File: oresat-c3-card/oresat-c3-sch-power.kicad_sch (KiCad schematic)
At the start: 68 parts, among them U31 LP2985AIM5-3.3, U34 TPS259621DDA, U35 TPS259620DDA, U36 LTC3624-5, U38 LP2985AIM5-3.3, U6 LTC3624-5

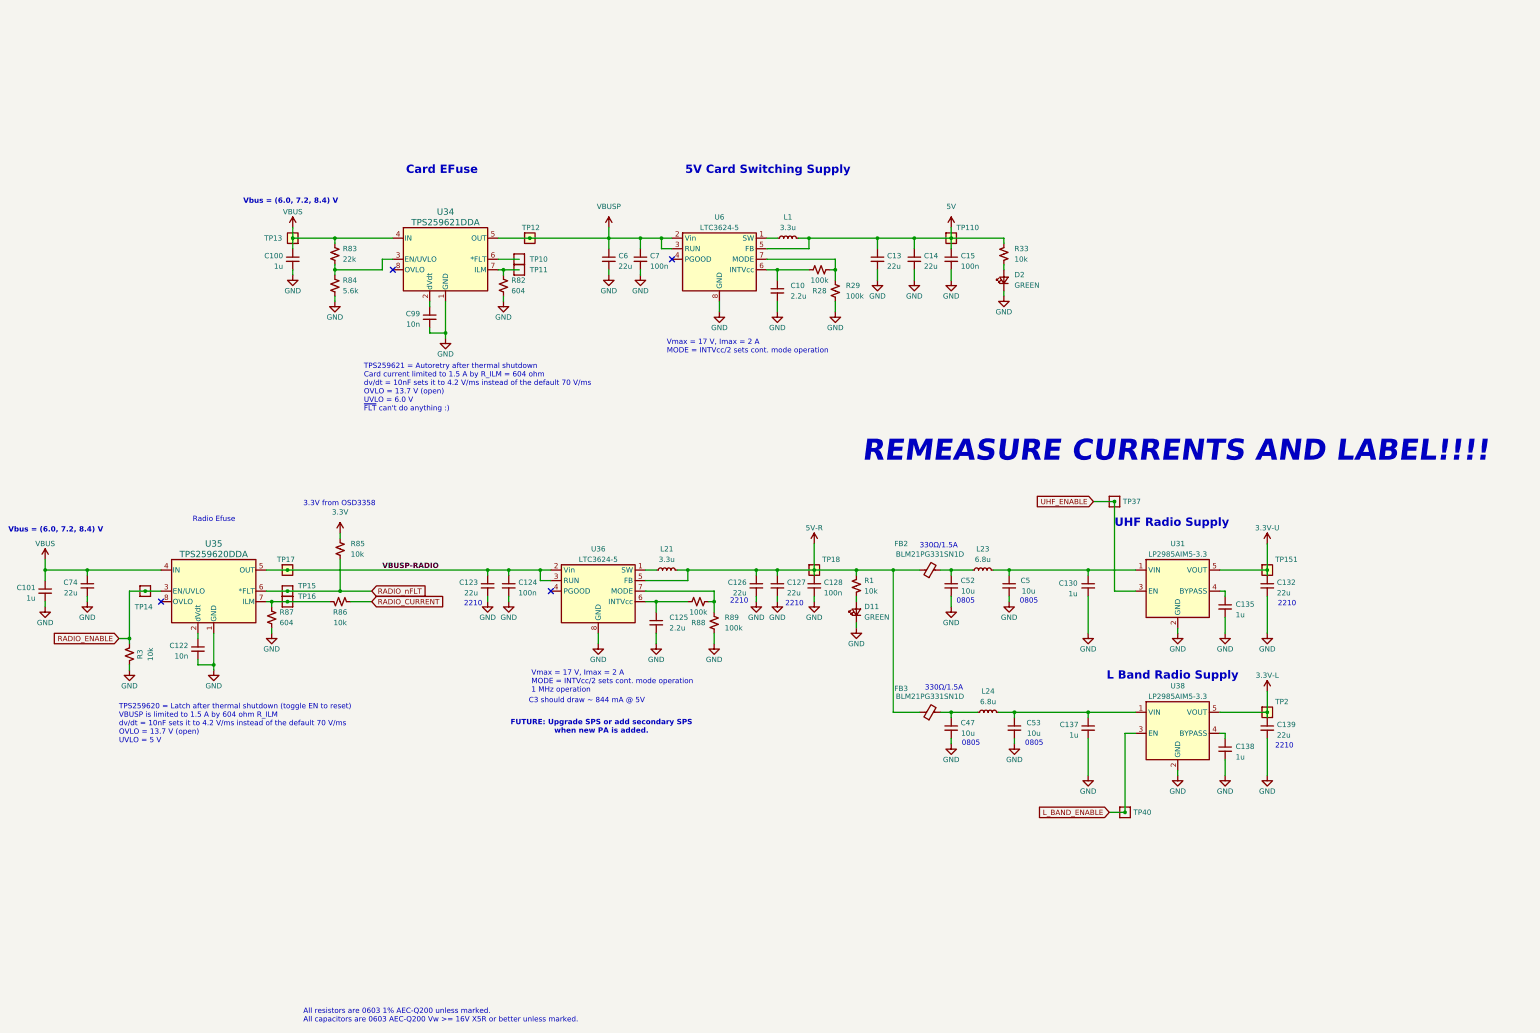
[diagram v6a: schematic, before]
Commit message: Updating BOM and switching to oresat-passive footprints. Fixed some power cutoff limits, and fixed another DC voltage leverl on an LNA!
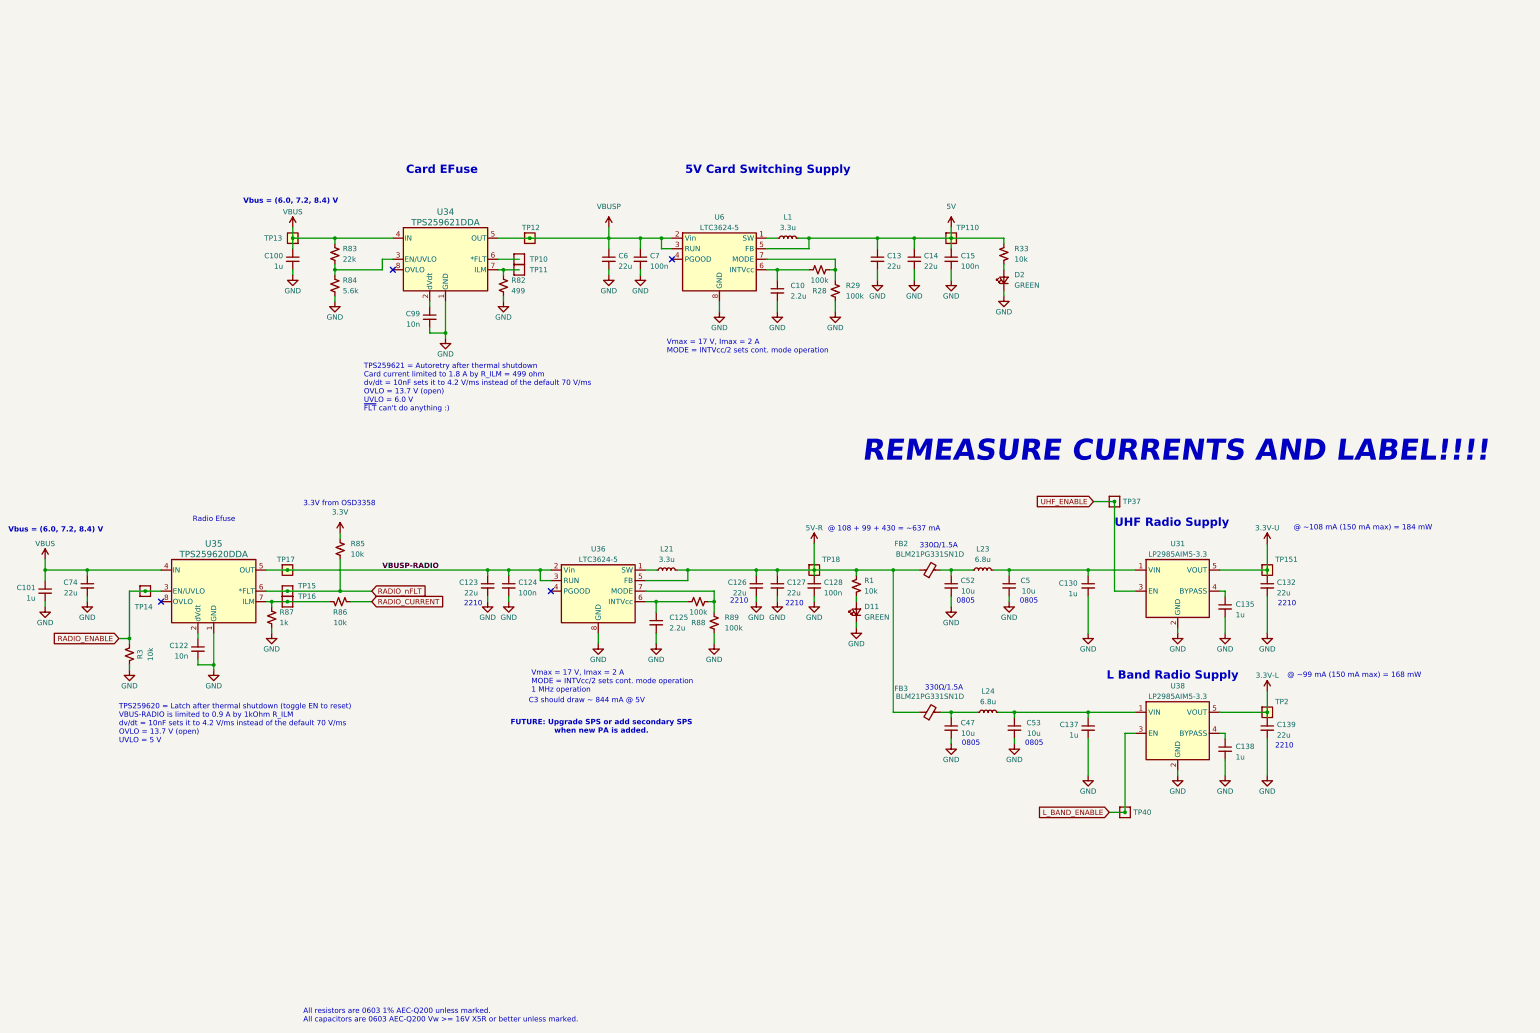
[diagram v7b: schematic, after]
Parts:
- C100, C101, C122, C124, C128, C130, C135, C137, C138, C15, C7, C99, D11, D2, FB2, FB3, L1, L21, L23, L24, U31, U34, U35, U36, U38, U6: DST Digi-Key -> DigiKey
- R1, R28, R29, R3, R33, R85, R86, R88, R89: footprint Resistor_SMD:R_0603_1608Metric -> oresat-passives:0603-C-NOSILK; DST Digi-Key -> DigiKey; MFR Stackpole Electronics Inc -> Stackpole Electronics
- R82: value 604 -> 499; footprint Resistor_SMD:R_0603_1608Metric -> oresat-passives:0603-C-NOSILK; DPN RMCF0603FT604RCT-ND -> RMCF0603FT499RCT-ND; DST Digi-Key -> DigiKey; MPN RMCF0603FT604R -> RMCF0603FT499R
- R83, R84: footprint Resistor_SMD:R_0603_1608Metric -> oresat-passives:0603-C-NOSILK; DST Digi-Key -> DigiKey
- R87: value 604 -> 1k; footprint Resistor_SMD:R_0603_1608Metric -> oresat-passives:0603-C-NOSILK; DPN RMCF0603FT604RCT-ND -> RMCF0603FT1K00CT-ND; DST Digi-Key -> DigiKey; MPN RMCF0603FT604R -> RMCF0603FT1K00
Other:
- note added: "@ 108 + 99 + 430 = ~637 mA"
- note added: "@ ~108 mA (150 mA max) = 184 mW"
- note added: "@ ~99 mA (150 mA max) = 168 mW"
- note added: "TPS259620 = Latch after thermal shutdown (toggle EN to reset) VBUS-RADIO is limited to 0.9 A by 1kOhm R_ILM dv/dt = 10nF sets it to 4.2 V/ms instead of the default 70 V/ms OVLO = 13.7 V (open) UVLO = 5 V"
- note added: "TPS259621 = Autoretry after thermal shutdown Card current limited to 1.8 A by R_ILM = 499 ohm dv/dt = 10nF sets it to 4.2 V/ms instead of the default 70 V/ms OVLO = 13.7 V (open) UVLO = 6.0 V ~{FLT} can't do anything :)"
- note removed: "TPS259620 = Latch after thermal shutdown (toggle EN to reset) VBUSP is limited to 1.5 A by 604 ohm R_ILM dv/dt = 10nF sets it to 4.2 V/ms instead of the default 70 V/ms OVLO = 13.7 V (open) UVLO = 5 V"
- note removed: "TPS259621 = Autoretry after thermal shutdown Card current limited to 1.5 A by R_ILM = 604 ohm dv/dt = 10nF sets it to 4.2 V/ms instead of the default 70 V/ms OVLO = 13.7 V (open) UVLO = 6.0 V ~{FLT} can't do anything :)"

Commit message: All footprints updated. Passes ERC/DRC.
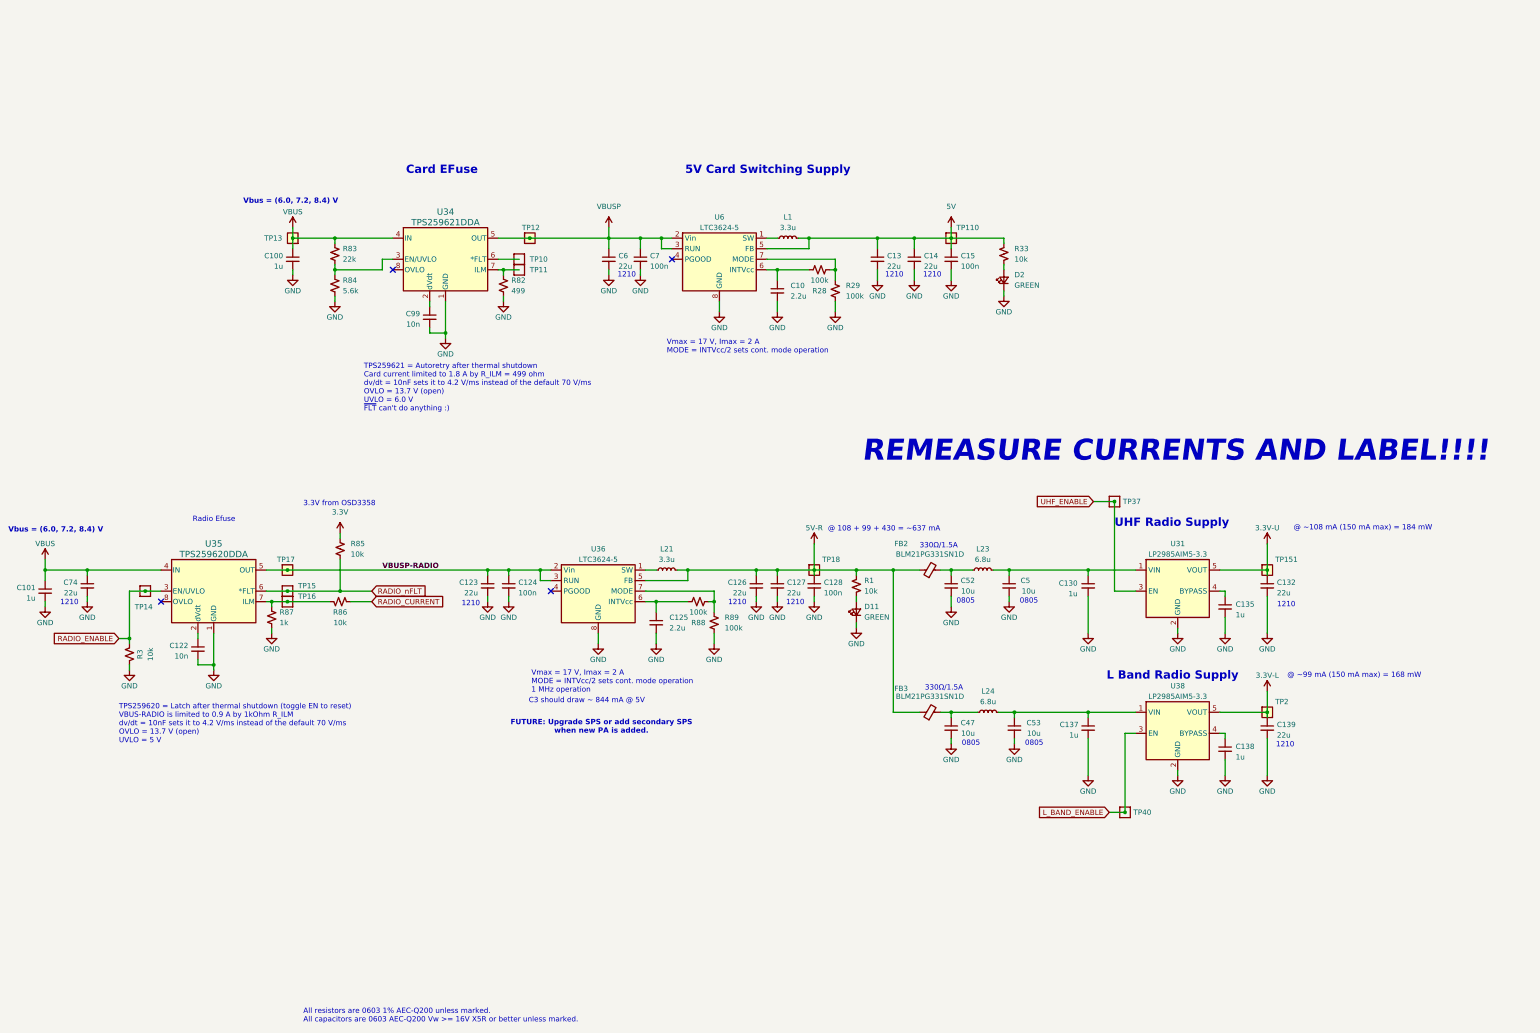
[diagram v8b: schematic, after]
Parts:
- C10, C125: footprint Capacitor_SMD:C_0603_1608Metric -> oresat-passives:0603-C-NOSILK; DPN 445-5959-1-ND -> 490-GRT188C71E225KE13DCT-ND; DST Digi-Key -> DigiKey; MFR TDK -> Murata Electronics; MPN C1608X7R1A225M080AC -> GRT188C71E225KE13D
- C100, C101, C130, C135, C137, C138: footprint Capacitor_SMD:C_0603_1608Metric -> oresat-passives:0603-C-NOSILK; DPN 587-3473-1-ND -> 490-GRT188R71E105KE13DCT-ND; MFR Taiyo Yuden -> Murata Electronics; MPN TMK107BJ105KAHT -> GRT188R71E105KE13D
- C122, C99: footprint Capacitor_SMD:C_0603_1608Metric -> oresat-passives:0603-C-NOSILK; DPN 399-14102-1-ND -> 399-12983-1-ND; MPN C0603C103J3GECAUTO -> C0603C103J5RACAUTO
- C123, C126, C127, C13, C132, C139, C14, C6, C74: DPN 490-GCM32EC71E226KE36KCT-ND -> 587-5949-1-ND; DST Digi-Key -> DigiKey; MFR Murata Electronics -> Taiyo Yuden; MPN GCM32EC71E226KE36K -> TMK325B7226KMHP
- C124, C128, C15, C7: footprint Capacitor_SMD:C_0603_1608Metric -> oresat-passives:0603-C-NOSILK; DPN 587-3472-1-ND -> 399-6856-1-ND; MFR Taiyo Yuden -> KEMET; MPN TMK107BJ104KAHT -> C0603C104K5RACAUTO
- C47, C5, C52, C53: footprint Capacitor_SMD:C_0805_2012Metric -> oresat-passives:0805-C-NOSILK; DPN 490-GRT21BC71E106KE13LCT-ND -> 490-GRT21BC71E106KE13KCT-ND; DST Digi-Key -> DigiKey; MPN GRT21BC71E106KE13L -> GRT21BC71E106KE13K
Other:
- note added: "1210"
- note removed: "2210"
